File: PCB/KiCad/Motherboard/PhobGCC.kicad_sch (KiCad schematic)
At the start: 66 parts, among them J1 Conn_01x06_Female, J2 Conn_01x04_Female, J3 Conn_01x01_Male, J5 Conn_01x02_Male, Q1 Q_NMOS_GSD, Q2 Q_PMOS_GDS, Q3 Q_NMOS_GSD, SW1 A, SW10 Dup, SW11 Dright, SW12 Ddown, SW2 B, SW3 X, SW4 Y, SW5 Start, SW6 L, SW7 R, SW8 Z, SW9 Dleft, U1 Teensy4.0, U2 2x DRV5053CAQLPGM Hall Effect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, U3 GP2S60-MFG, U4 GP2S60-MFG

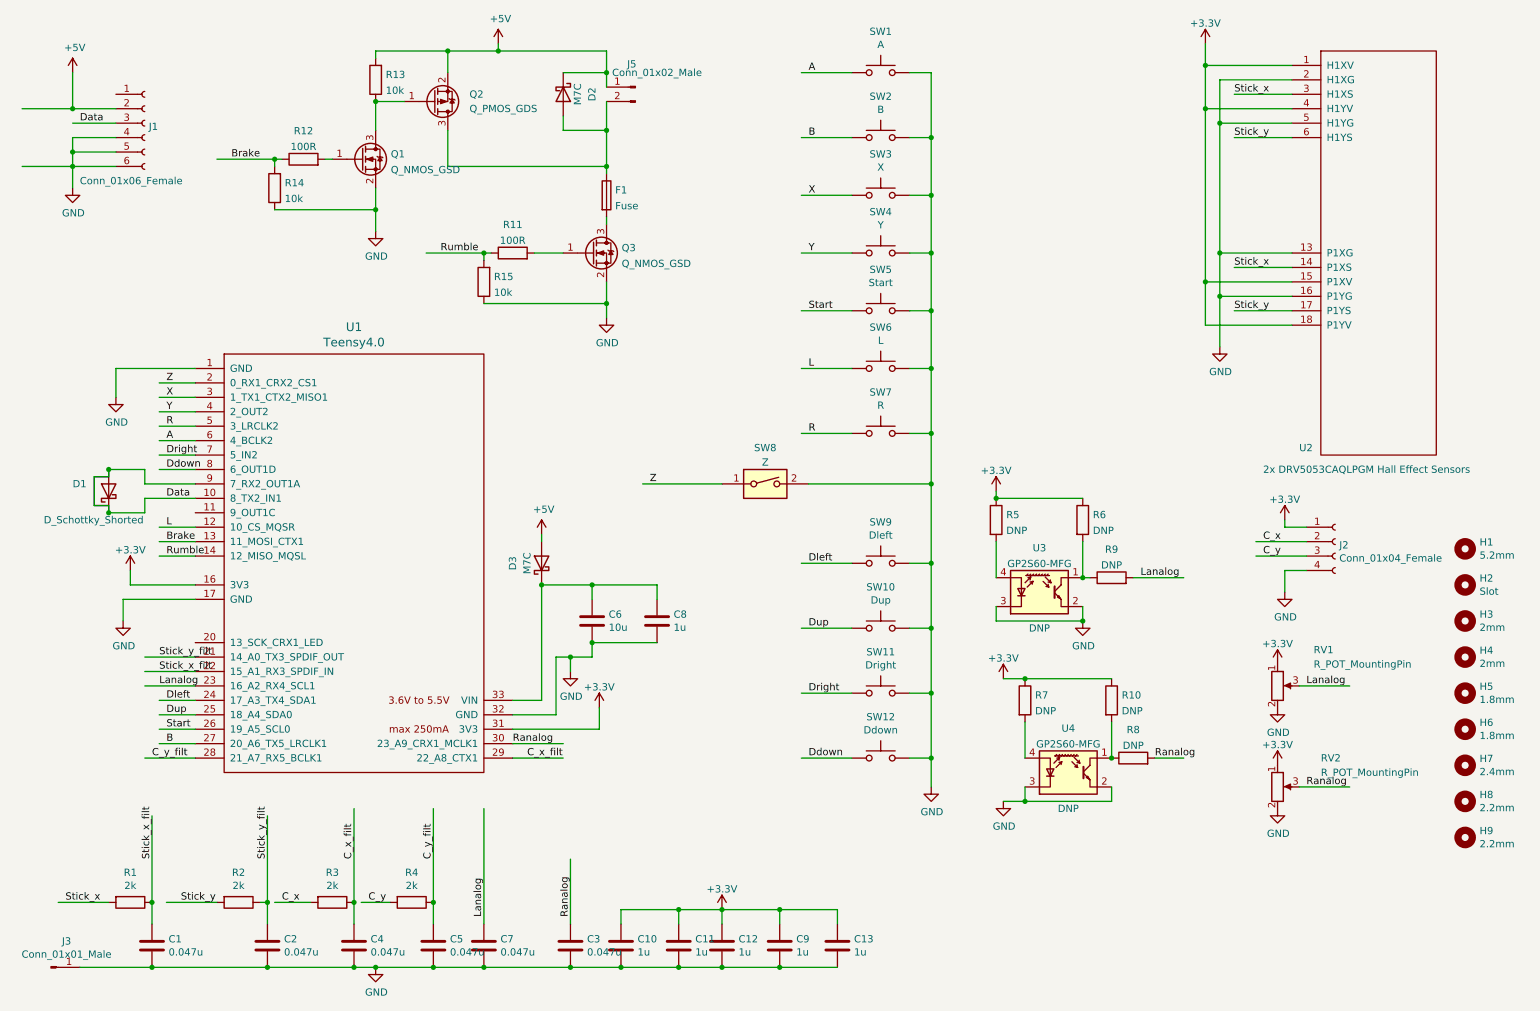
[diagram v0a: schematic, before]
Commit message: Replaced teensy 4 with pico stamp and completed basic schematic and layout changes
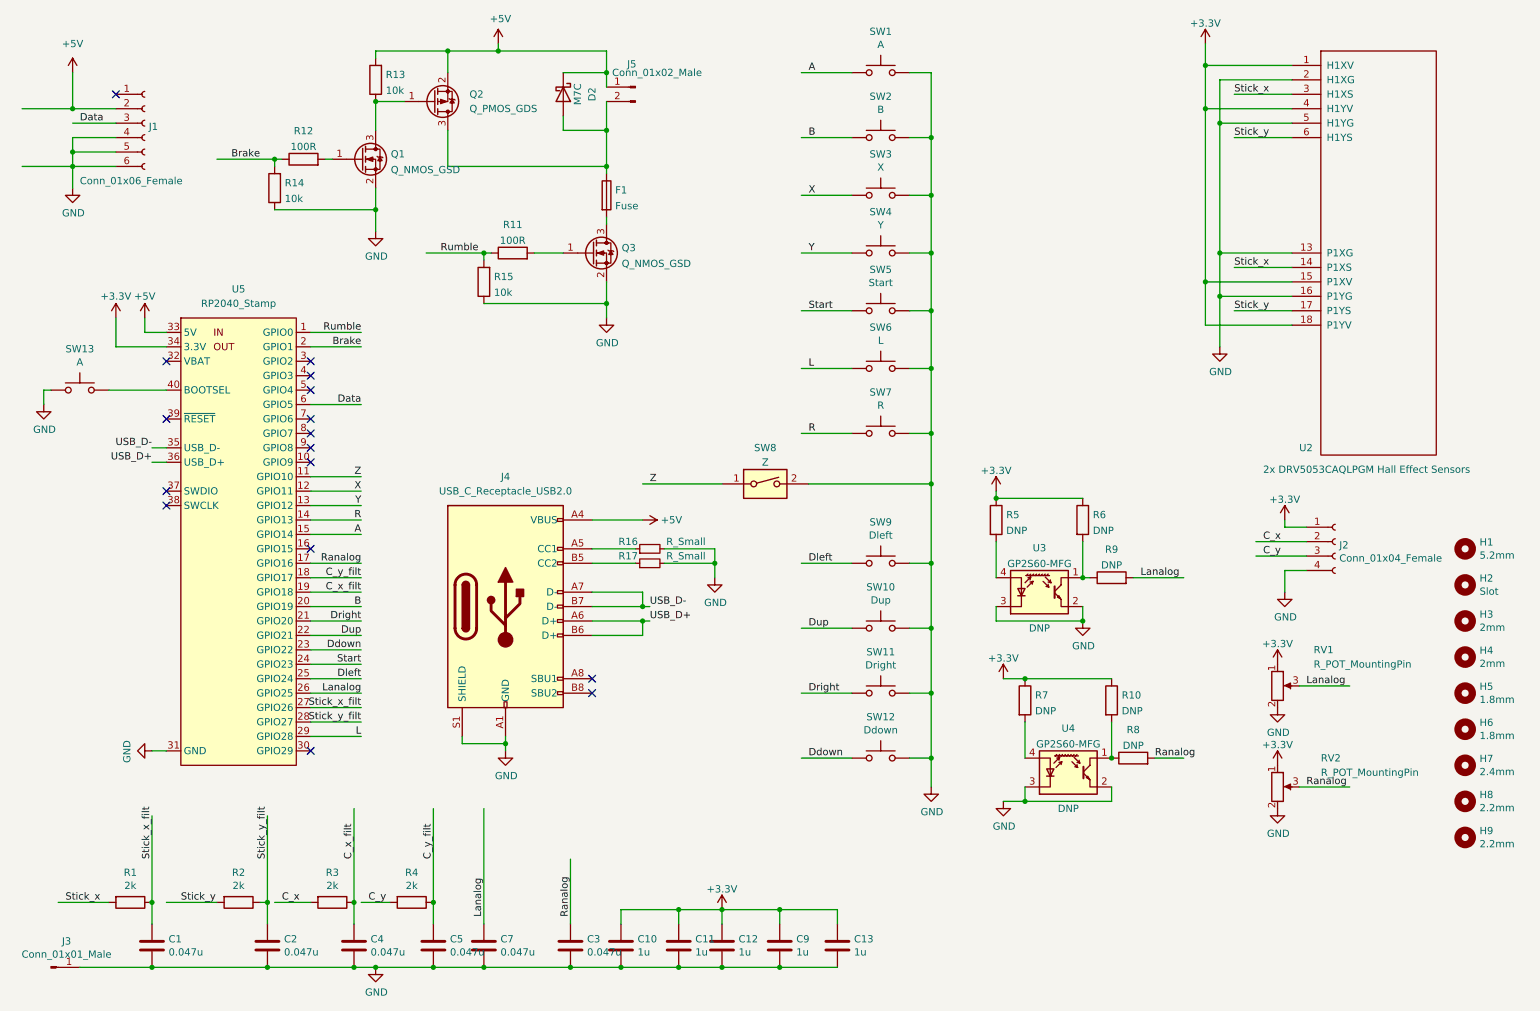
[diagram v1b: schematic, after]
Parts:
- removed C6: 10u, PhobGCC_Footprints:C_0603_HandSoldering, symbol Device:C
- removed C8: 1u, PhobGCC_Footprints:C_0603_1608Metric_Pad1.08x0.95mm_HandSolder, symbol Device:C
- removed D1: D_Schottky_Shorted, PhobGCC_Footprints:D_SOD-523_Shorted, symbol Gamecube MB:D_Schottky_Shorted
- removed D3: M7C, PhobGCC_Footprints:D_SOD-123, symbol Device:D_Schottky
- removed U1: Teensy4.0, PhobGCC_Footprints:Teensy40_Edge_Pins, symbol teensy:Teensy4.0
- added J4: USB_C_Receptacle_USB2.0, USB4155-03-C_REVA:GCT_USB4155-03-C_REVA, symbol Connector:USB_C_Receptacle_USB2.0
- added R16, R17: R_Small, Resistor_SMD:R_0603_1608Metric_Pad0.98x0.95mm_HandSolder, symbol Device:R_Small
- added SW13: A, PhobGCC_Footprints:ABXY_Contact_Omron_Switch, symbol Switch:SW_Push
- added U5: RP2040_Stamp, RP2040_Stamp:RP2040_Stamp_SMD, symbol RP2040_Stamp:RP2040_Stamp
- SW8: footprint (none) -> PhobGCC_Footprints:Z_Switch_Edge_Omron
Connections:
- net +3V3: now also U5.34 (3.3V)
- net +5V: now also J4.A4 (VBUS), J4.A9 (VBUS), J4.B4 (VBUS), J4.B9 (VBUS), U5.33 (5V)
- net A: now also U5.15 (GPIO14)
- net B: now also U5.20 (GPIO19)
- net Brake: now also U5.2 (GPIO1)
- net C_x_filt: now also U5.19 (GPIO18)
- net C_y_filt: now also U5.18 (GPIO17)
- net Data: now also U5.6 (GPIO5)
- net Ddown: now also U5.23 (GPIO22)
- net Dleft: now also U5.25 (GPIO24)
- net Dright: now also U5.21 (GPIO20)
- net Dup: now also U5.22 (GPIO21)
- net GND: now also J4.A1 (GND), J4.A12 (GND), J4.B1 (GND), J4.B12 (GND), J4.S1 (SHIELD), R16.2, R17.2, SW13.1, U5.31 (GND)
- net L: now also U5.29 (GPIO28)
- net Lanalog: now also U5.26 (GPIO25)
- net R: now also U5.14 (GPIO13)
- net Ranalog: now also U5.17 (GPIO16)
- net Rumble: now also U5.1 (GPIO0)
- net Start: now also U5.24 (GPIO23)
- net Stick_x_filt: now also U5.27 (GPIO26)
- net Stick_y_filt: now also U5.28 (GPIO27)
- net X: now also U5.12 (GPIO11)
- net Y: now also U5.13 (GPIO12)
- net Z: now also U5.11 (GPIO10)
- new net: J4.A5 (CC1), R16.1
- new net: J4.B5 (CC2), R17.1
- new net: SW13.2, U5.40 (BOOTSEL)
- new net USB_D+: J4.A6 (D+), J4.B6 (D+), U5.36 (USB_D+)
- new net USB_D-: J4.A7 (D-), J4.B7 (D-), U5.35 (USB_D-)
- no-connect marks 0 -> 16
